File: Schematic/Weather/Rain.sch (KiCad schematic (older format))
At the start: 0 parts

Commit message: more changes
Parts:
- added J7: 4_Way_Wire, Connector_PinHeader_2.54mm:PinHeader_1x04_P2.54mm_Vertical, symbol MyComponents:4_Way_Wire
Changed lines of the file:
@@
 $Descr A4 11693 8268
 encoding utf-8
-Sheet 8 14
+Sheet 7 15
 Title ""
 Date ""
@@
 Text HLabel 2500 2100 0    50   Input ~ 0
 J11_P4
+$Comp
+L MyComponents:4_Way_Wire J7
+U 1 1 5CB4C8FC
+P 3350 1500
+F 0 "J7" H 3519 1261 50  0000 L CNN
+F 1 "4_Way_Wire" H 3519 1170 50  0000 L CNN
+F 2 "Connector_PinHeader_2.54mm:PinHeader_1x04_P2.54mm_Vertical" H 3250 1550 50  0001 C CNN
+F 3 "" H 3250 1550 50  0001 C CNN
+	1    3350 1500
+	1    0    0    -1
+$EndComp
 $EndSCHEMATC

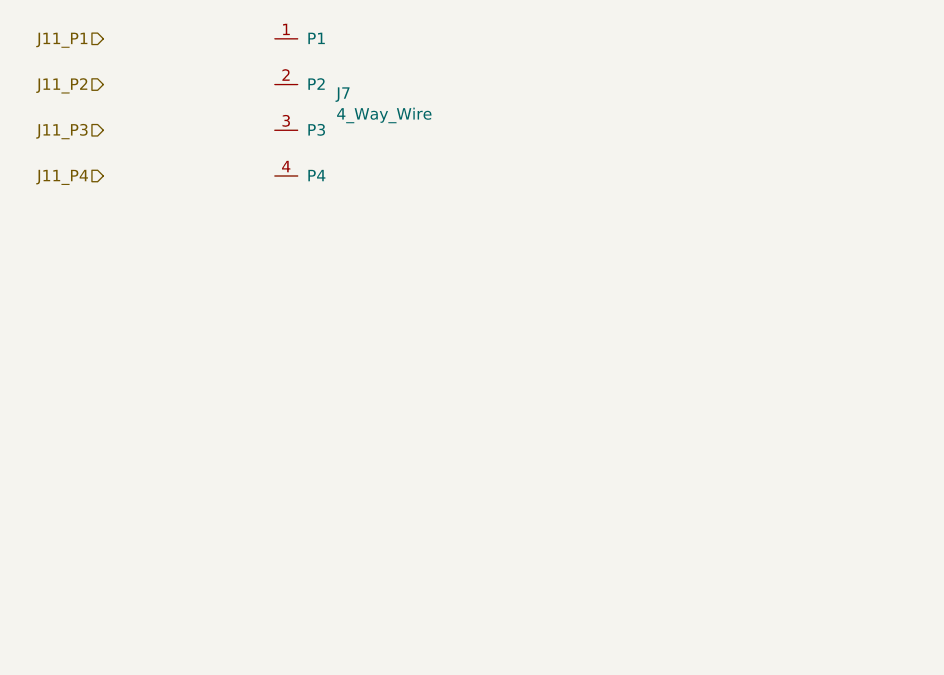
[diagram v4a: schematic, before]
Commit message: Connector relable start
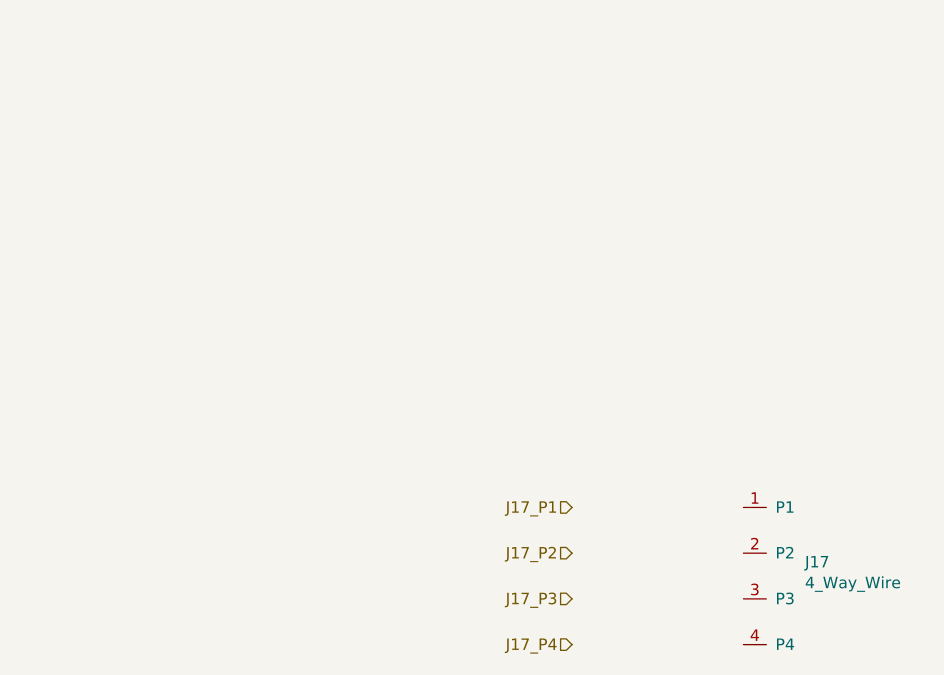
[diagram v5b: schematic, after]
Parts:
- renumbered J7 to J17
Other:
- moved on the sheet: J17
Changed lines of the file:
@@
 $Descr A4 11693 8268
 encoding utf-8
-Sheet 7 15
+Sheet 15 15
 Title ""
 Date ""
@@
 Comment4 ""
 $EndDescr
-Text HLabel 2500 1500 0    50   Input ~ 0
-J11_P1
-Text HLabel 2500 1700 0    50   Input ~ 0
-J11_P2
-Text HLabel 2500 1900 0    50   Input ~ 0
-J11_P3
-Text HLabel 2500 2100 0    50   Input ~ 0
-J11_P4
+Text HLabel 4550 3550 0    50   Input ~ 0
+J17_P1
+Text HLabel 4550 3750 0    50   Input ~ 0
+J17_P2
+Text HLabel 4550 3950 0    50   Input ~ 0
+J17_P3
+Text HLabel 4550 4150 0    50   Input ~ 0
+J17_P4
 $Comp
-L MyComponents:4_Way_Wire J7
+L MyComponents:4_Way_Wire J17
 U 1 1 5CB4C8FC
-P 3350 1500
-F 0 "J7" H 3519 1261 50  0000 L CNN
-F 1 "4_Way_Wire" H 3519 1170 50  0000 L CNN
-F 2 "Connector_PinHeader_2.54mm:PinHeader_1x04_P2.54mm_Vertical" H 3250 1550 50  0001 C CNN
-F 3 "" H 3250 1550 50  0001 C CNN
-	1    3350 1500
+P 5400 3550
+F 0 "J17" H 5569 3311 50  0000 L CNN
+F 1 "4_Way_Wire" H 5569 3220 50  0000 L CNN
+F 2 "Connector_PinHeader_2.54mm:PinHeader_1x04_P2.54mm_Vertical" H 5300 3600 50  0001 C CNN
+F 3 "" H 5300 3600 50  0001 C CNN
+	1    5400 3550
 	1    0    0    -1
 $EndComp

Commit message: schm update
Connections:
- net J17_P1: now also J17.1 (P1)
- net J17_P2: now also J17.2 (P2)
- net J17_P3: now also J17.3 (P3)
- net J17_P4: now also J17.4 (P4)
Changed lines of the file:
@@
 	1    0    0    -1
 $EndComp
+Wire Wire Line
+	4550 3550 5300 3550
+Wire Wire Line
+	4550 3750 5300 3750
+Wire Wire Line
+	4550 3950 5300 3950
+Wire Wire Line
+	4550 4150 5300 4150
 $EndSCHEMATC
